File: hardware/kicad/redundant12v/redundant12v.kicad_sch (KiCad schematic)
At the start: 26 parts, among them J1 22-12-2064, J2 IDC 2x5 Male, Q1 SMMBT3904LT1G, Q2 SMMBT3904LT1G, U1 ATTINY212-SSF, U2 MAX232CPE, U3 LD1117S50CTR, X1 ECS-3951M-018-AU-TR

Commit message: Replace Maxim MAX232ECWE+T with TI MAX232EID for narrower SOIC-16
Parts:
- U2: value MAX232CPE -> TI MAX232EID
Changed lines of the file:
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@@
       (effects (font (size 1.27 1.27)) (justify left))
     )
-    (property "Value" "MAX232CPE" (id 1) (at 186.1694 71.12 0)
+    (property "Value" "TI MAX232EID" (id 1) (at 186.1694 71.12 0)
       (effects (font (size 1.27 1.27)) (justify left))
     )
@@
     )
     (path "/07decc8d-143b-433a-959b-b8fccf779f4d"
-      (reference "U2") (unit 1) (value "MAX232CPE") (footprint "Package_SO:SOIC-16_3.9x9.9mm_P1.27mm")
+      (reference "U2") (unit 1) (value "TI MAX232EID") (footprint "Package_SO:SOIC-16_3.9x9.9mm_P1.27mm")
     )
     (path "/7835d074-be50-46e8-aa67-f1fb94cafd58"

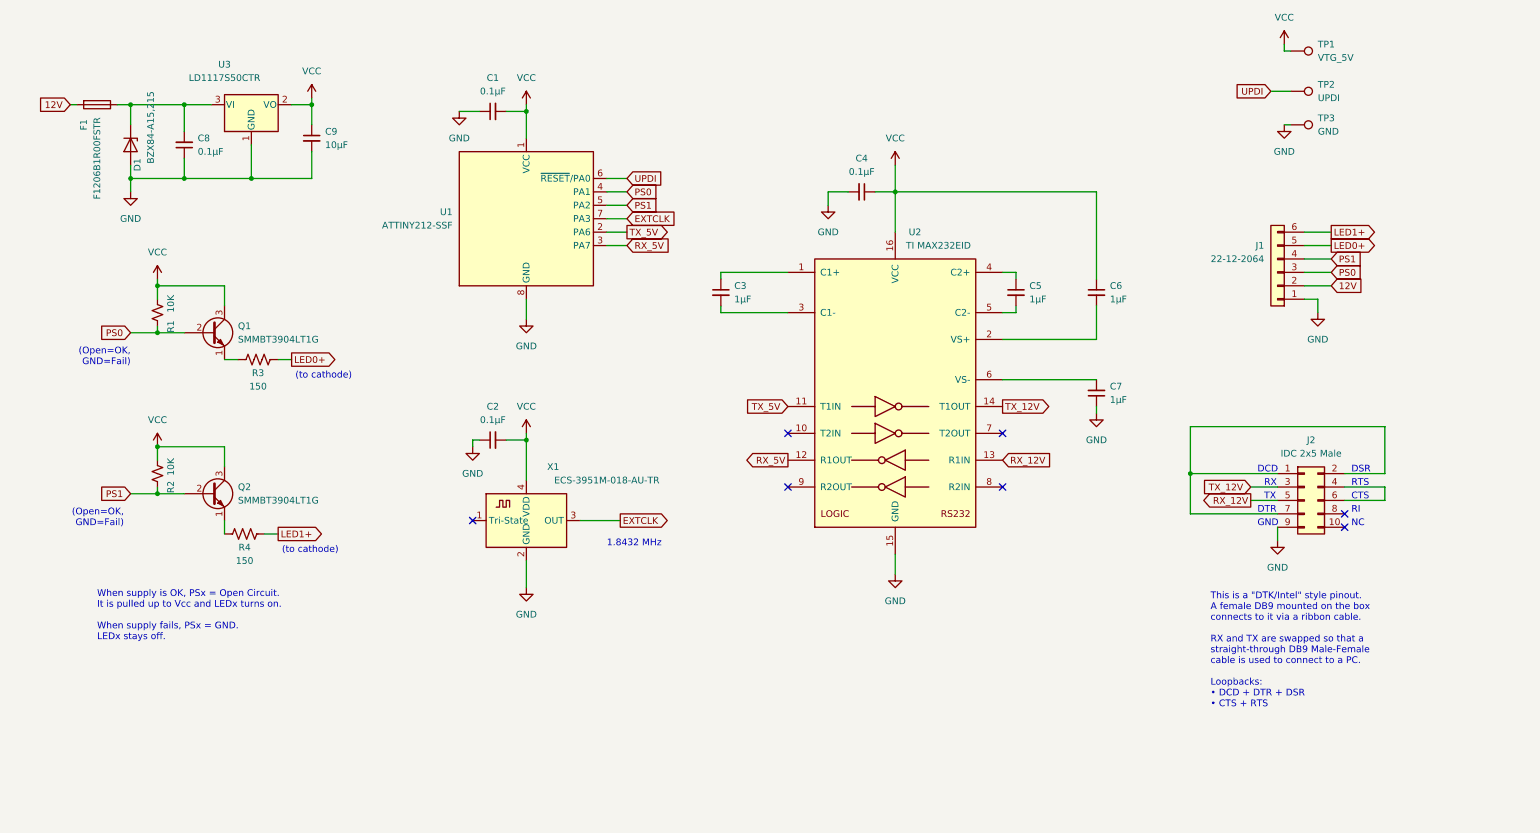
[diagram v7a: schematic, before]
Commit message: Fix alarm detection, rotate serial connector
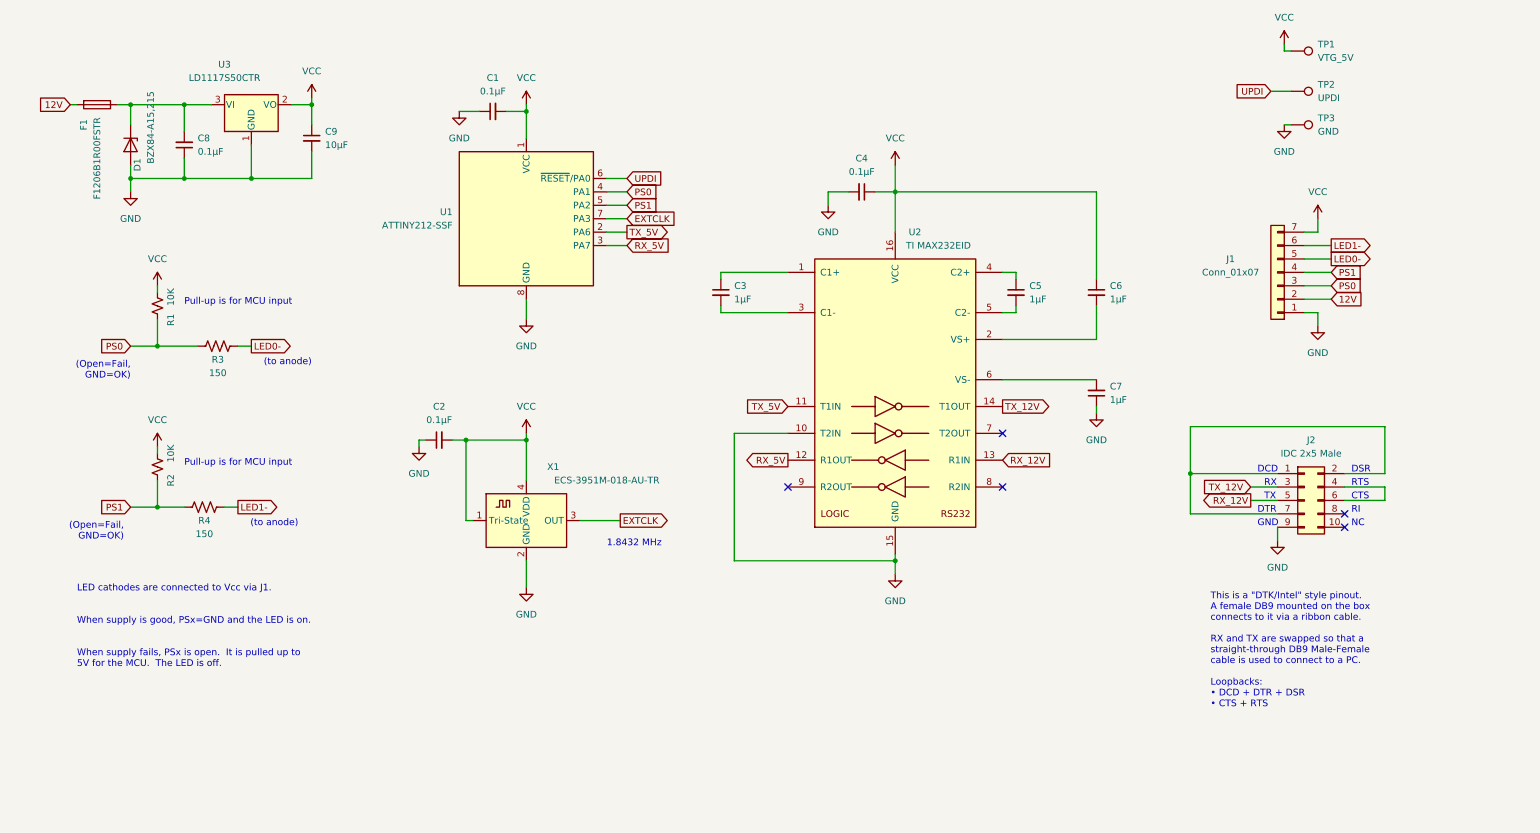
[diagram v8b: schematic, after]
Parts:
- removed J1: 22-12-2064, Connector_JST:JST_EH_B6B-EH-A_1x06_P2.50mm_Vertical, symbol Connector_Generic:Conn_01x06
- removed Q1, Q2: SMMBT3904LT1G, Package_TO_SOT_SMD:SOT-23, symbol Transistor_BJT:2N3904
- added J1: Conn_01x07, Connector_Molex:Molex_KK-254_AE-6410-07A_1x07_P2.54mm_Vertical, symbol Connector_Generic:Conn_01x07
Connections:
- net 12V: now also J1.2 (Pin_2)
- net GND: now also U2.10 (T2IN), J1.1 (Pin_1)
- net PS0: now also R3.1, J1.3 (Pin_3)
- net PS1: now also R4.1, J1.4 (Pin_4)
- net VCC: now also X1.1 (Tri-State), J1.7 (Pin_7)
- net LED0+ renamed LED0-
- net LED0-: now also J1.5 (Pin_5)
- net LED1+ renamed LED1-
- net LED1-: now also J1.6 (Pin_6)
- no-connect marks 7 -> 5
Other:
- note added: "(Open=Fail, GND=OK)"
- note added: "(to anode)"
- note added: "LED cathodes are connected to Vcc via J1. When supply is good, PSx=GND and the LED is on. When supply fails, PSx is open. It is pulled up to 5V for the MCU. The LED is off."
- note added: "Pull-up is for MCU input"
- note removed: "(Open=OK, GND=Fail)"
- note removed: "(to cathode)"
- note removed: "When supply is OK, PSx = Open Circuit. It is pulled up to Vcc and LEDx turns on. When supply fails, PSx = GND. LEDx stays off."
- moved on the sheet: C2, R1, R2, R3, R4
